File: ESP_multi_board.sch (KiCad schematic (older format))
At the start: 32 parts, among them IC101 L298, P101 CONN_01X02, P102 CONN_01X06, P103 CONN_01X02, P104 CONN_01X06, P105 CONN_01X12, P106 CONN_01X03, P107 CONN_I2C_MPU6050, P108 CONN_PINES_DIG, SW101 SW_PUSH_SMALL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

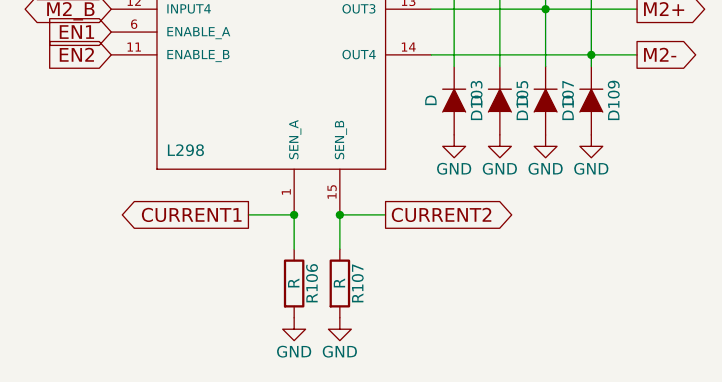
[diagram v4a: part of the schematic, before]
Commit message: asignadas huellas diodos, provisionales
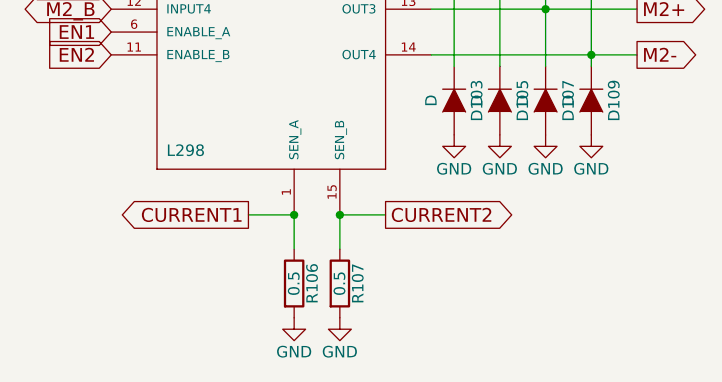
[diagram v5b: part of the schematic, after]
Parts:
- D101: footprint Diodes_ThroughHole:Diode_DO-35_SOD27_Horizontal_RM10 -> Diodes_SMD:D-Pak_TO252AA
- D102, D103, D104, D105, D106, D107, D108, D109: footprint (none) -> Diodes_SMD:D-Pak_TO252AA
- R106, R107: value R -> 0.5; footprint (none) -> Resistors_SMD:R_1206

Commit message: huellas diodos actualizadas
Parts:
- P105: symbol CONN_01X12 -> CONN_01X10
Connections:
- net CURRENT1: now also U103.1 (Ain11_/_REF)
- net CURRENT2: now also U103.2 (Ain10)
- no-connect marks 5 -> 7
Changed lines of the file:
@@
 SCL
 $Comp
-L CONN_01X12 P105
+L CONN_01X10 P105
 U 1 1 57125BDF
-P 3650 5100
-F 0 "P105" H 3650 5750 50  0000 C CNN
-F 1 "CONN_01X12" V 3750 5100 50  0000 C CNN
-F 2 "Pin_Headers:Pin_Header_Straight_1x12" H 3650 5100 50  0001 C CNN
-F 3 "" H 3650 5100 50  0000 C CNN
-	1    3650 5100
+P 3650 5200
+F 0 "P105" H 3650 5850 50  0000 C CNN
+F 1 "CONN_01X12" V 3750 5200 50  0000 C CNN
+F 2 "Pin_Headers:Pin_Header_Straight_1x12" H 3650 5200 50  0001 C CNN
+F 3 "" H 3650 5200 50  0000 C CNN
+	1    3650 5200
 	-1   0    0    1
 $EndComp
@@
 $EndComp
 Wire Wire Line
-	3950 4450 4450 4450
-Wire Wire Line
-	3950 4450 3950 4550
-Wire Wire Line
-	3850 4650 4450 4650
+	3850 4450 4450 4450
 Wire Wire Line
 	4450 4850 4350 4850
@@
 Wire Wire Line
 	3950 5550 3850 5550
-Wire Wire Line
-	3950 4550 3850 4550
 Wire Wire Line
 	9150 1950 9700 1950
@@
 	2200 5350 3100 5350
 Wire Wire Line
-	3100 5550 2200 5550
-Wire Wire Line
-	3100 5750 2200 5750
+	2200 5550 3100 5550
+Wire Wire Line
+	2200 5750 3100 5750
 $Comp
 L GND #PWR026
@@
 Connection ~ 2700 5550
 Connection ~ 2900 5750
+NoConn ~ 2350 2950
+NoConn ~ 1700 8400
+Text GLabel 3850 4450 0    60   Input ~ 0
+CURRENT1
+Text GLabel 3850 4600 0    60   Input ~ 0
+CURRENT2
+Wire Wire Line
+	4450 4650 4050 4650
+Wire Wire Line
+	4050 4650 4050 4600
+Wire Wire Line
+	4050 4600 3850 4600
 $EndSCHEMATC

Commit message: organizacion directorio
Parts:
- D101, D102, D103, D104, D105, D106, D107, D108, D109: footprint Diodes_SMD:D-Pak_TO252AA -> SMD_Packages:SMD-1206_Pol
- P105: footprint Pin_Headers:Pin_Header_Straight_1x12 -> Pin_Headers:Pin_Header_Straight_1x10
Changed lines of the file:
@@
 LIBS:contrib
 LIBS:valves
-LIBS:ESP8266
-LIBS:stepper drivers
-LIBS:mpu-6050
-LIBS:MCP23008
-LIBS:microchip_adcdac
-LIBS:ESP_multi_board-cache
 EELAYER 25 0
 EELAYER END
@@
 F 0 "P105" H 3650 5850 50  0000 C CNN
 F 1 "CONN_01X12" V 3750 5200 50  0000 C CNN
-F 2 "Pin_Headers:Pin_Header_Straight_1x12" H 3650 5200 50  0001 C CNN
+F 2 "Pin_Headers:Pin_Header_Straight_1x10" H 3650 5200 50  0001 C CNN
 F 3 "" H 3650 5200 50  0000 C CNN
 	1    3650 5200
@@
 F 0 "D101" H 1150 2950 50  0000 C CNN
 F 1 "D" H 1150 2750 50  0000 C CNN
-F 2 "Diodes_SMD:D-Pak_TO252AA" H 1150 2850 50  0001 C CNN
+F 2 "SMD_Packages:SMD-1206_Pol" H 1150 2850 50  0001 C CNN
 F 3 "" H 1150 2850 50  0000 C CNN
 	1    1150 2850
@@
 F 0 "D103" H 2300 6050 50  0000 C CNN
 F 1 "D" H 2300 5850 50  0000 C CNN
-F 2 "Diodes_SMD:D-Pak_TO252AA" H 2300 5950 50  0001 C CNN
+F 2 "SMD_Packages:SMD-1206_Pol" H 2300 5950 50  0001 C CNN
 F 3 "" H 2300 5950 50  0000 C CNN
 	1    2300 5950
@@
 F 0 "D105" H 2500 6050 50  0000 C CNN
 F 1 "D" H 2500 5850 50  0000 C CNN
-F 2 "Diodes_SMD:D-Pak_TO252AA" H 2500 5950 50  0001 C CNN
+F 2 "SMD_Packages:SMD-1206_Pol" H 2500 5950 50  0001 C CNN
 F 3 "" H 2500 5950 50  0000 C CNN
 	1    2500 5950
@@
 F 0 "D107" H 2700 6050 50  0000 C CNN
 F 1 "D" H 2700 5850 50  0000 C CNN
-F 2 "Diodes_SMD:D-Pak_TO252AA" H 2700 5950 50  0001 C CNN
+F 2 "SMD_Packages:SMD-1206_Pol" H 2700 5950 50  0001 C CNN
 F 3 "" H 2700 5950 50  0000 C CNN
 	1    2700 5950
@@
 F 0 "D109" H 2900 6050 50  0000 C CNN
 F 1 "D" H 2900 5850 50  0000 C CNN
-F 2 "Diodes_SMD:D-Pak_TO252AA" H 2900 5950 50  0001 C CNN
+F 2 "SMD_Packages:SMD-1206_Pol" H 2900 5950 50  0001 C CNN
 F 3 "" H 2900 5950 50  0000 C CNN
 	1    2900 5950
@@
 F 0 "D102" H 2300 5050 50  0000 C CNN
 F 1 "D" H 2300 4850 50  0000 C CNN
-F 2 "Diodes_SMD:D-Pak_TO252AA" H 2300 4950 50  0001 C CNN
+F 2 "SMD_Packages:SMD-1206_Pol" H 2300 4950 50  0001 C CNN
 F 3 "" H 2300 4950 50  0000 C CNN
 	1    2300 4950
@@
 F 0 "D104" H 2500 5050 50  0000 C CNN
 F 1 "D" H 2500 4850 50  0000 C CNN
-F 2 "Diodes_SMD:D-Pak_TO252AA" H 2500 4950 50  0001 C CNN
+F 2 "SMD_Packages:SMD-1206_Pol" H 2500 4950 50  0001 C CNN
 F 3 "" H 2500 4950 50  0000 C CNN
 	1    2500 4950
@@
 F 0 "D106" H 2700 5050 50  0000 C CNN
 F 1 "D" H 2700 4850 50  0000 C CNN
-F 2 "Diodes_SMD:D-Pak_TO252AA" H 2700 4950 50  0001 C CNN
+F 2 "SMD_Packages:SMD-1206_Pol" H 2700 4950 50  0001 C CNN
 F 3 "" H 2700 4950 50  0000 C CNN
 	1    2700 4950
@@
 F 0 "D108" H 2900 5050 50  0000 C CNN
 F 1 "D" H 2900 4850 50  0000 C CNN
-F 2 "Diodes_SMD:D-Pak_TO252AA" H 2900 4950 50  0001 C CNN
+F 2 "SMD_Packages:SMD-1206_Pol" H 2900 4950 50  0001 C CNN
 F 3 "" H 2900 4950 50  0000 C CNN
 	1    2900 4950
